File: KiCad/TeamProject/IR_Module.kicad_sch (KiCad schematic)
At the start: 20 parts, among them U1 MCP6294, U4 MCP6294, U4 MCP6546, U6 MCP6294

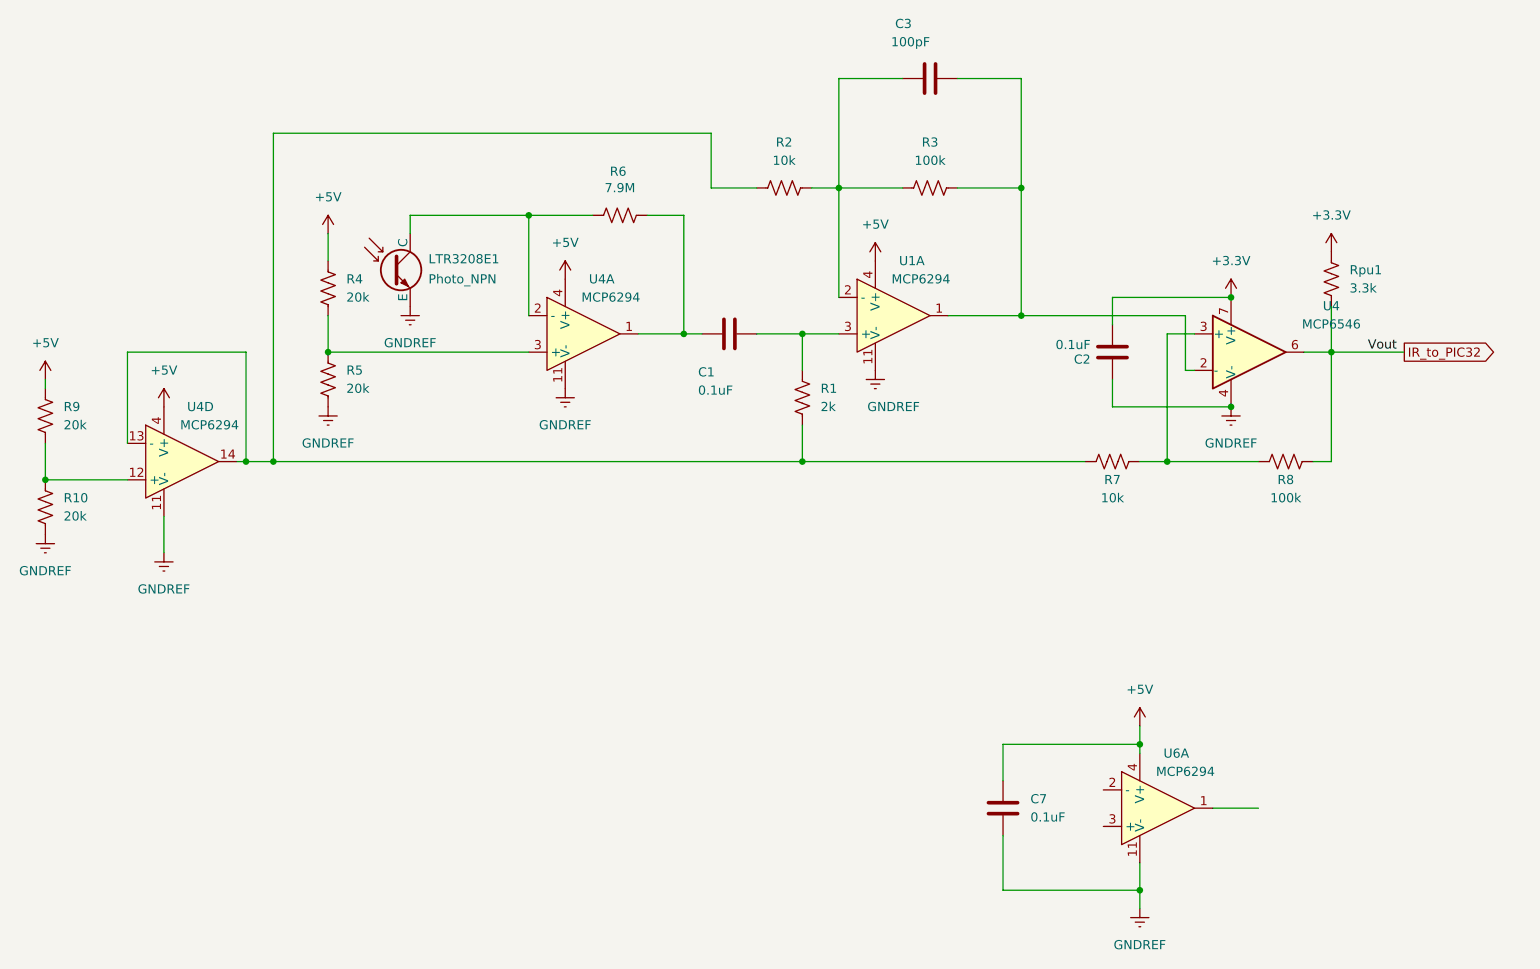
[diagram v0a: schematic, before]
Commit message: Match IR with reality
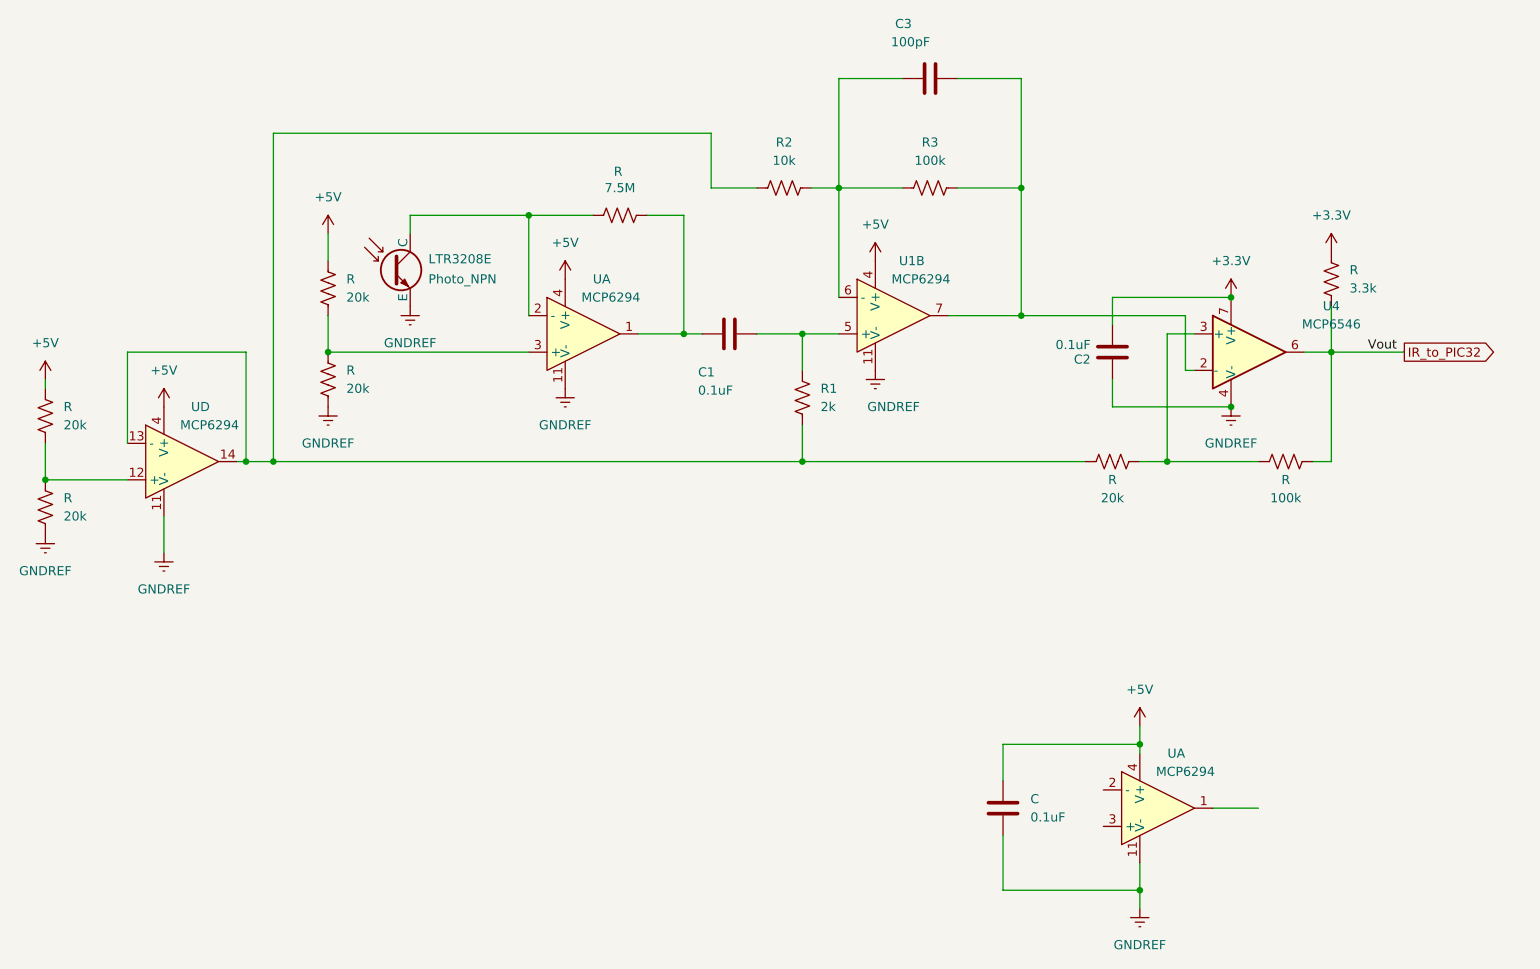
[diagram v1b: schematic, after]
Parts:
- R: renamed from R7; value 10k -> 20k
- R: renamed from R6; value 7.9M -> 7.5M
- renumbered C7 to C, LTR3208E1 to LTR3208E, R8 to R, R9 to R, Rpu1 to R, R10 to R, R5 to R, R4 to R, U4 to U, U6 to U
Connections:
- net at C3.1, R3.2, U4.2 (-): now also U1.7; no longer U1.1
- net at C3.2, R2.2, R3.1: now also U1.6 (-); no longer U1.2 (-)
- net at C1.1, R1.2: now also U1.5 (+); no longer U1.3 (+)
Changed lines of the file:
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@@
 		(on_board yes)
 		(dnp no)
-		(property "Reference" "#PWR?"
+		(property "Reference" "#PWR02"
 			(at 166.37 90.17 0)
 			(effects
@@
 		(on_board yes)
 		(dnp no)
-		(property "Reference" "C?"
+		(property "Reference" "C2"
 			(at 196.342 82.296 0)
 			(effects
@@
 		(lib_id "ME218_BaseLib:MCP6294")
 		(at 168.91 76.2 0)
-		(unit 1)
-		(exclude_from_sim no)
-		(in_bom yes)
-		(on_board yes)
-		(dnp no)
-		(property "Reference" "U?"
+		(unit 2)
+		(exclude_from_sim no)
+		(in_bom yes)
+		(on_board yes)
+		(dnp no)
+		(property "Reference" "U1"
 			(at 171.45 68.58 0)
 			(effects
@@
 		(on_board yes)
 		(dnp no)
-		(property "Reference" "R7"
+		(property "Reference" "R"
 			(at 199.39 99.06 90)
 			(effects
@@
 			)
 		)
-		(property "Value" "10k"
+		(property "Value" "20k"
 			(at 199.39 101.6 90)
 			(effects
@@
 		(dnp no)
 		(fields_autoplaced yes)
-		(property "Reference" "R?"
+		(property "Reference" "R3"
 			(at 173.99 52.07 90)
 			(effects
@@
 		(dnp no)
 		(fields_autoplaced yes)
-		(property "Reference" "R?"
+		(property "Reference" "R1"
 			(at 158.75 86.3599 0)
 			(effects
@@
 		(dnp no)
 		(fields_autoplaced yes)
-		(property "Reference" "#PWR?"
+		(property "Reference" "#PWR03"
 			(at 101.6 81.28 0)
 			(effects
@@
 		(dnp no)
 		(fields_autoplaced yes)
-		(property "Reference" "#PWR09"
+		(property "Reference" "#PWR?"
 			(at 90.17 95.25 0)
 			(effects
@@
 		(on_board yes)
 		(dnp no)
-		(property "Reference" "R8"
+		(property "Reference" "R"
 			(at 223.52 99.06 90)
 			(effects
@@
 		(dnp no)
 		(fields_autoplaced yes)
-		(property "Reference" "R9"
+		(property "Reference" "R"
 			(at 53.34 88.8999 0)
 			(effects
@@
 		(dnp no)
 		(fields_autoplaced yes)
-		(property "Reference" "#PWR?"
+		(property "Reference" "#PWR01"
 			(at 166.37 72.39 0)
 			(effects
@@
 		(on_board yes)
 		(dnp no)
-		(property "Reference" "U?"
+		(property "Reference" "U4"
 			(at 229.87 74.8598 0)
 			(effects
@@
 		(dnp no)
 		(fields_autoplaced yes)
-		(property "Reference" "#PWR029"
+		(property "Reference" "#PWR?"
 			(at 215.9 77.47 0)
 			(effects
@@
 		(dnp no)
 		(fields_autoplaced yes)
-		(property "Reference" "#PWR032"
+		(property "Reference" "#PWR?"
 			(at 67.31 115.57 0)
 			(effects
@@
 		(on_board yes)
 		(dnp no)
-		(property "Reference" "C?"
+		(property "Reference" "C1"
 			(at 144.018 84.074 90)
 			(effects
@@
 		(dnp no)
 		(fields_autoplaced yes)
-		(property "Reference" "#PWR023"
+		(property "Reference" "#PWR?"
 			(at 123.19 74.93 0)
 			(effects
@@
 		(on_board yes)
 		(dnp no)
-		(property "Reference" "C?"
+		(property "Reference" "C3"
 			(at 171.45 35.56 90)
 			(effects
@@
 		(dnp no)
 		(fields_autoplaced yes)
-		(property "Reference" "C7"
+		(property "Reference" "C"
 			(at 187.96 143.5099 0)
 			(effects
@@
 		(dnp no)
 		(fields_autoplaced yes)
-		(property "Reference" "#PWR030"
+		(property "Reference" "#PWR?"
 			(at 215.9 95.25 0)
 			(effects
@@
 		(dnp no)
 		(fields_autoplaced yes)
-		(property "Reference" "#PWR024"
+		(property "Reference" "#PWR?"
 			(at 123.19 92.71 0)
 			(effects
@@
 		(dnp no)
 		(fields_autoplaced yes)
-		(property "Reference" "#PWR021"
+		(property "Reference" "#PWR?"
 			(at 50.8 113.03 0)
 			(effects
@@
 		(dnp no)
 		(fields_autoplaced yes)
-		(property "Reference" "#PWR031"
+		(property "Reference" "#PWR?"
 			(at 67.31 92.71 0)
 			(effects
@@
 		(on_board yes)
 		(dnp no)
-		(property "Reference" "U4"
+		(property "Reference" "U"
 			(at 72.39 88.9 0)
 			(effects
@@
 		(dnp no)
 		(fields_autoplaced yes)
-		(property "Reference" "#PWR020"
+		(property "Reference" "#PWR?"
 			(at 50.8 88.9 0)
 			(effects
@@
 		(dnp no)
 		(fields_autoplaced yes)
-		(property "Reference" "Rpu1"
+		(property "Reference" "R"
 			(at 232.41 69.8499 0)
 			(effects
@@
 		(on_board yes)
 		(dnp no)
-		(property "Reference" "LTR3208E1"
+		(property "Reference" "LTR3208E"
 			(at 104.14 68.326 0)
 			(effects
@@
 		(dnp no)
 		(fields_autoplaced yes)
-		(property "Reference" "R10"
+		(property "Reference" "R"
 			(at 53.34 101.5999 0)
 			(effects
@@
 		(on_board yes)
 		(dnp no)
-		(property "Reference" "R6"
+		(property "Reference" "R"
 			(at 130.556 56.134 90)
 			(effects
@@
 			)
 		)
-		(property "Value" "7.9M"
+		(property "Value" "7.5M"
 			(at 130.81 58.42 90)
 			(effects
@@
 		(on_board yes)
 		(dnp no)
-		(property "Reference" "U4"
+		(property "Reference" "U"
 			(at 128.27 71.12 0)
 			(effects
@@
 		(dnp no)
 		(fields_autoplaced yes)
-		(property "Reference" "R5"
+		(property "Reference" "R"
 			(at 92.71 83.8199 0)
 			(effects
@@
 		(dnp no)
 		(fields_autoplaced yes)
-		(property "Reference" "#PWR027"
+		(property "Reference" "#PWR?"
 			(at 229.87 71.12 0)
 			(effects
@@
 		(dnp no)
 		(fields_autoplaced yes)
-		(property "Reference" "#PWR025"
+		(property "Reference" "#PWR?"
 			(at 203.2 137.16 0)
 			(effects
@@
 		(dnp no)
 		(fields_autoplaced yes)
-		(property "Reference" "#PWR026"
+		(property "Reference" "#PWR?"
 			(at 203.2 165.1 0)
 			(effects
@@
 		(on_board yes)
 		(dnp no)
-		(property "Reference" "U6"
+		(property "Reference" "U"
 			(at 208.28 137.16 0)
 			(effects
@@
 		(dnp no)
 		(fields_autoplaced yes)
-		(property "Reference" "#PWR08"
+		(property "Reference" "#PWR?"
 			(at 90.17 68.58 0)
 			(effects
@@
 		(dnp no)
 		(fields_autoplaced yes)
-		(property "Reference" "R4"
+		(property "Reference" "R"
 			(at 92.71 71.1199 0)
 			(effects
@@
 		(dnp no)
 		(fields_autoplaced yes)
-		(property "Reference" "R?"
+		(property "Reference" "R2"
 			(at 153.67 52.07 90)
 			(effects

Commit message: Merge branch 'main' of https://github.com/ttyaaron/ME218B_TeamProject
# Conflicts:
#	LeaderPIC.X/ProjectSource/CommonDefinitions.c
#	LeaderPIC.X/build/default/debug/ProjectSource/BeaconDetectFSM.o
#	LeaderPIC.X/build/default/debug/ProjectSource/CommonDefinitions.o
#	LeaderPIC.X/build/default/debug/ProjectSource/DCMotorService.o
#	LeaderPIC.X/build/default/debug/ProjectSource/EventCheckers.o
#	LeaderPIC.X/build/default/debug/ProjectSource/MainLogicFSM.o
#	LeaderPIC.X/build/default/debug/ProjectSource/SPILeaderFSM.o
#	LeaderPIC.X/build/default/debug/ProjectSource/TestHarnessService0.o
#	LeaderPIC.X/build/default/production/ProjectSource/BeaconDetectFSM.o
#	LeaderPIC.X/build/default/production/ProjectSource/CommonDefinitions.o
#	LeaderPIC.X/build/default/production/ProjectSource/DCMotorService.o
#	LeaderPIC.X/build/default/production/ProjectSource/EventCheckers.o
#	LeaderPIC.X/build/default/production/ProjectSource/MainLogicFSM.o
#	LeaderPIC.X/build/default/production/ProjectSource/SPILeaderFSM.o
#	LeaderPIC.X/build/default/production/ProjectSource/TestHarnessService0.o
#	LeaderPIC.X/dist/default/debug/LeaderPIC.X.debug.elf
#	LeaderPIC.X/dist/default/debug/LeaderPIC.X.debug.map
#	LeaderPIC.X/dist/default/debug/memoryfile.xml
#	LeaderPIC.X/dist/default/production/LeaderPIC.X.production.elf
#	LeaderPIC.X/dist/default/production/LeaderPIC.X.production.hex
#	LeaderPIC.X/dist/default/production/LeaderPIC.X.production.map
#	LeaderPIC.X/dist/default/production/memoryfile.xml
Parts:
- renumbered C to C7, LTR3208E to LTR3208E1, R to R10, R to R4, R to R5, R to R6, R to R7, R to R8, R to R9, R to Rpu1, U to U4, U to U6
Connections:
- net at C1.1, R1.2: now also U1.3 (+); no longer U1.5 (+)
- net at C3.2, R2.2, R3.1: now also U1.2 (-); no longer U1.6 (-)
- net at C3.1, R3.2, U4.2 (-): now also U1.1; no longer U1.7
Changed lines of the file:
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@@
 		(on_board yes)
 		(dnp no)
-		(property "Reference" "#PWR02"
+		(property "Reference" "#PWR?"
 			(at 166.37 90.17 0)
 			(effects
@@
 		(on_board yes)
 		(dnp no)
-		(property "Reference" "C2"
+		(property "Reference" "C?"
 			(at 196.342 82.296 0)
 			(effects
@@
 		(lib_id "ME218_BaseLib:MCP6294")
 		(at 168.91 76.2 0)
-		(unit 2)
-		(exclude_from_sim no)
-		(in_bom yes)
-		(on_board yes)
-		(dnp no)
-		(property "Reference" "U1"
+		(unit 1)
+		(exclude_from_sim no)
+		(in_bom yes)
+		(on_board yes)
+		(dnp no)
+		(property "Reference" "U?"
 			(at 171.45 68.58 0)
 			(effects
@@
 		(on_board yes)
 		(dnp no)
-		(property "Reference" "R"
+		(property "Reference" "R7"
 			(at 199.39 99.06 90)
 			(effects
@@
 		(dnp no)
 		(fields_autoplaced yes)
-		(property "Reference" "R3"
+		(property "Reference" "R?"
 			(at 173.99 52.07 90)
 			(effects
@@
 		(dnp no)
 		(fields_autoplaced yes)
-		(property "Reference" "R1"
+		(property "Reference" "R?"
 			(at 158.75 86.3599 0)
 			(effects
@@
 		(dnp no)
 		(fields_autoplaced yes)
-		(property "Reference" "#PWR03"
+		(property "Reference" "#PWR?"
 			(at 101.6 81.28 0)
 			(effects
@@
 		(dnp no)
 		(fields_autoplaced yes)
-		(property "Reference" "#PWR?"
+		(property "Reference" "#PWR09"
 			(at 90.17 95.25 0)
 			(effects
@@
 		(on_board yes)
 		(dnp no)
-		(property "Reference" "R"
+		(property "Reference" "R8"
 			(at 223.52 99.06 90)
 			(effects
@@
 		(dnp no)
 		(fields_autoplaced yes)
-		(property "Reference" "R"
+		(property "Reference" "R9"
 			(at 53.34 88.8999 0)
 			(effects
@@
 		(dnp no)
 		(fields_autoplaced yes)
-		(property "Reference" "#PWR01"
+		(property "Reference" "#PWR?"
 			(at 166.37 72.39 0)
 			(effects
@@
 		(on_board yes)
 		(dnp no)
-		(property "Reference" "U4"
+		(property "Reference" "U?"
 			(at 229.87 74.8598 0)
 			(effects
@@
 		(dnp no)
 		(fields_autoplaced yes)
-		(property "Reference" "#PWR?"
+		(property "Reference" "#PWR029"
 			(at 215.9 77.47 0)
 			(effects
@@
 		(dnp no)
 		(fields_autoplaced yes)
-		(property "Reference" "#PWR?"
+		(property "Reference" "#PWR032"
 			(at 67.31 115.57 0)
 			(effects
@@
 		(on_board yes)
 		(dnp no)
-		(property "Reference" "C1"
+		(property "Reference" "C?"
 			(at 144.018 84.074 90)
 			(effects
@@
 		(dnp no)
 		(fields_autoplaced yes)
-		(property "Reference" "#PWR?"
+		(property "Reference" "#PWR023"
 			(at 123.19 74.93 0)
 			(effects
@@
 		(on_board yes)
 		(dnp no)
-		(property "Reference" "C3"
+		(property "Reference" "C?"
 			(at 171.45 35.56 90)
 			(effects
@@
 		(dnp no)
 		(fields_autoplaced yes)
-		(property "Reference" "C"
+		(property "Reference" "C7"
 			(at 187.96 143.5099 0)
 			(effects
@@
 		(dnp no)
 		(fields_autoplaced yes)
-		(property "Reference" "#PWR?"
+		(property "Reference" "#PWR030"
 			(at 215.9 95.25 0)
 			(effects
@@
 		(dnp no)
 		(fields_autoplaced yes)
-		(property "Reference" "#PWR?"
+		(property "Reference" "#PWR024"
 			(at 123.19 92.71 0)
 			(effects
@@
 		(dnp no)
 		(fields_autoplaced yes)
-		(property "Reference" "#PWR?"
+		(property "Reference" "#PWR021"
 			(at 50.8 113.03 0)
 			(effects
@@
 		(dnp no)
 		(fields_autoplaced yes)
-		(property "Reference" "#PWR?"
+		(property "Reference" "#PWR031"
 			(at 67.31 92.71 0)
 			(effects
@@
 		(on_board yes)
 		(dnp no)
-		(property "Reference" "U"
+		(property "Reference" "U4"
 			(at 72.39 88.9 0)
 			(effects
@@
 		(dnp no)
 		(fields_autoplaced yes)
-		(property "Reference" "#PWR?"
+		(property "Reference" "#PWR020"
 			(at 50.8 88.9 0)
 			(effects
@@
 		(dnp no)
 		(fields_autoplaced yes)
-		(property "Reference" "R"
+		(property "Reference" "Rpu1"
 			(at 232.41 69.8499 0)
 			(effects
@@
 		(on_board yes)
 		(dnp no)
-		(property "Reference" "LTR3208E"
+		(property "Reference" "LTR3208E1"
 			(at 104.14 68.326 0)
 			(effects
@@
 		(dnp no)
 		(fields_autoplaced yes)
-		(property "Reference" "R"
+		(property "Reference" "R10"
 			(at 53.34 101.5999 0)
 			(effects
@@
 		(on_board yes)
 		(dnp no)
-		(property "Reference" "R"
+		(property "Reference" "R6"
 			(at 130.556 56.134 90)
 			(effects
@@
 		(on_board yes)
 		(dnp no)
-		(property "Reference" "U"
+		(property "Reference" "U4"
 			(at 128.27 71.12 0)
 			(effects
@@
 		(dnp no)
 		(fields_autoplaced yes)
-		(property "Reference" "R"
+		(property "Reference" "R5"
 			(at 92.71 83.8199 0)
 			(effects
@@
 		(dnp no)
 		(fields_autoplaced yes)
-		(property "Reference" "#PWR?"
+		(property "Reference" "#PWR027"
 			(at 229.87 71.12 0)
 			(effects
@@
 		(dnp no)
 		(fields_autoplaced yes)
-		(property "Reference" "#PWR?"
+		(property "Reference" "#PWR025"
 			(at 203.2 137.16 0)
 			(effects
@@
 		(dnp no)
 		(fields_autoplaced yes)
-		(property "Reference" "#PWR?"
+		(property "Reference" "#PWR026"
 			(at 203.2 165.1 0)
 			(effects
@@
 		(on_board yes)
 		(dnp no)
-		(property "Reference" "U"
+		(property "Reference" "U6"
 			(at 208.28 137.16 0)
 			(effects
@@
 		(dnp no)
 		(fields_autoplaced yes)
-		(property "Reference" "#PWR?"
+		(property "Reference" "#PWR08"
 			(at 90.17 68.58 0)
 			(effects
@@
 		(dnp no)
 		(fields_autoplaced yes)
-		(property "Reference" "R"
+		(property "Reference" "R4"
 			(at 92.71 71.1199 0)
 			(effects
@@
 		(dnp no)
 		(fields_autoplaced yes)
-		(property "Reference" "R2"
+		(property "Reference" "R?"
 			(at 153.67 52.07 90)
 			(effects
